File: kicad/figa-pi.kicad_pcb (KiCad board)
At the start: 4 copper layers, 65 x 56 mm, 158 parts, among them J1 BH-10(IDC-10MS), J2 PLS-2, J3 PBD-40(DS1023-2x20), J4 PLD-10(DS1021-2x5), J5 L829-1J1T-43, J6 POE connector, J7 PLS-1, J8 PLS-1, J9 PLS-1, U1 24LC32A/SN, U10 TLV62084DSGR, U11 TLV62084DSGR, U2 ASEMB-25.000MHZ-LC-T, U3 NUP4114UPXV6T1G, U5 10CL025ZE144, U6 KSZ9021GN, U7 CDCLVC1102PW, U9 TLV62084DSGR

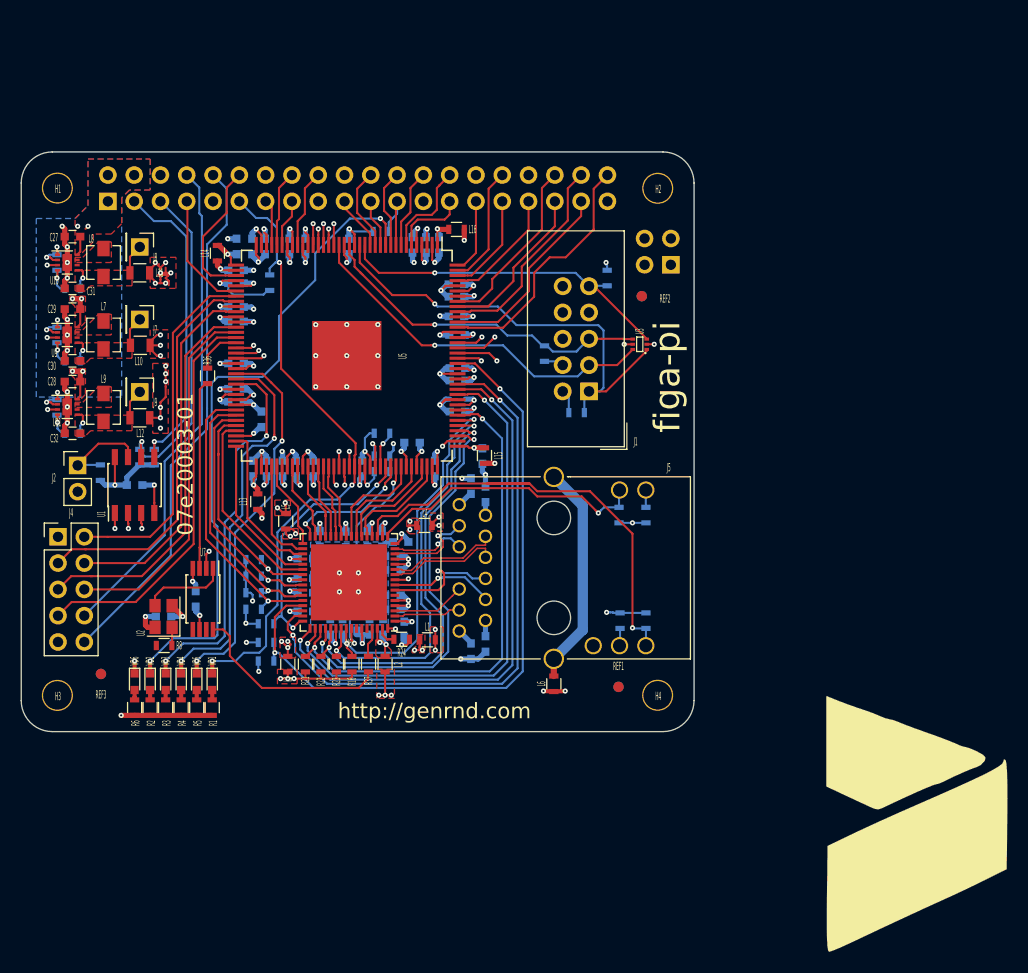
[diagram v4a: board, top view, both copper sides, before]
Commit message: Added logo as 2 footprints Corrected RefDes dimensions and placement on silk layers
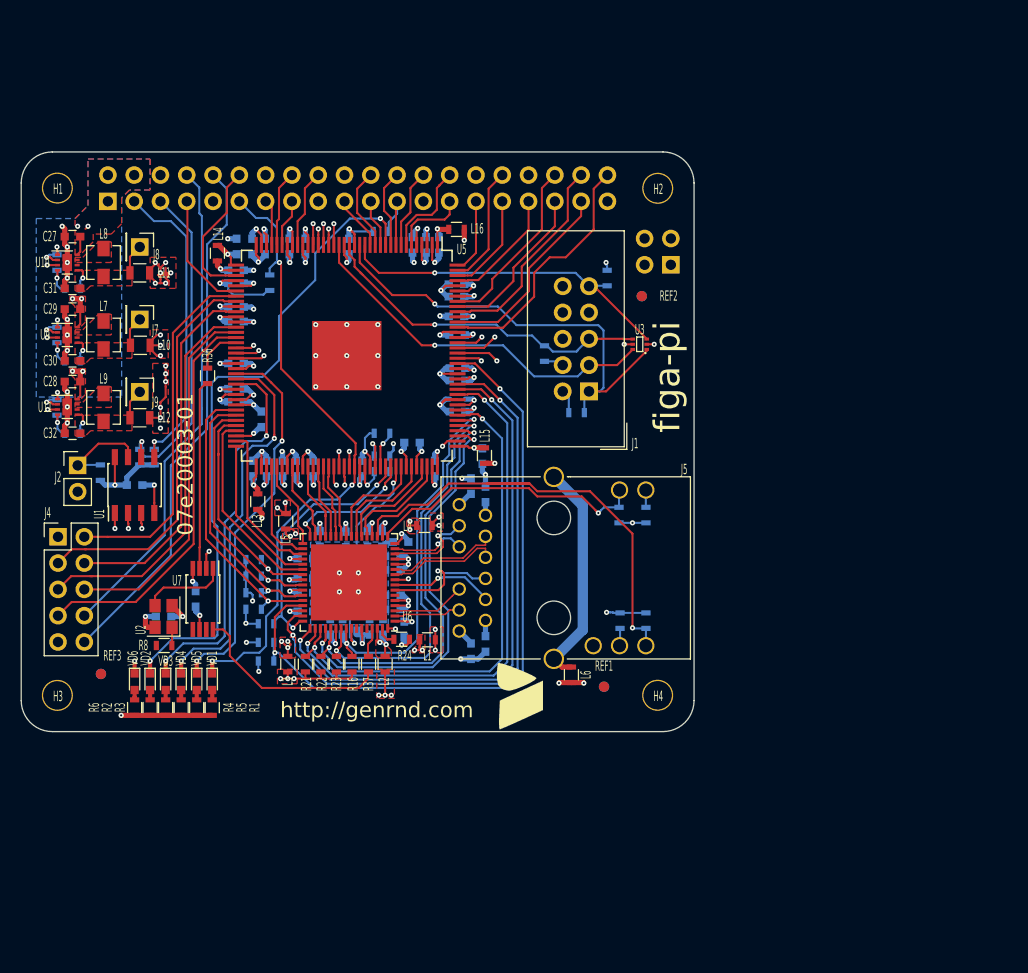
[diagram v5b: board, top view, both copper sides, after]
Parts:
- removed the G*** at (165.1, 125.7)
- added G***: LOGO, project_footprints:Logo_25_1, F.Cu at (126.3, 111.5)
- added G***: LOGO, project_footprints:Logo_25_2, F.Cu at (126.7, 114.1)
- moved L6 1.91 mm to (131.7, 111.3)
- moved REF1 1.40 mm to (134.8, 112.5)
- moved REF5 1.40 mm to (134.8, 112.5)
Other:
- rule pad_to_mask_clearance: 0.1 -> 0.05
- board text added: "This is a HAT compatible PCB starting design based on the official Raspberry Pi specs at: https://github.com/raspberrypi/hats/blob/master/designguide.md"
- board text removed: "If you want to use an SMT 40-pin header, please move the top edge up by 0.5mm and locate the header in the same location as the current TH part."
- board text removed: "This is a HAT compatible PCB starting design based on the official Raspberry Pi specs at: https://github.com/raspberrypi/hats/blob/master/designguide.md Currently the camera slot and display cutout are not here. See the schematic for the details on the EEPROM and power setup. This board does have the correct components for powering the Pi via the HAT. If you need the Pi to provide 5V or 3.3V, ple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"

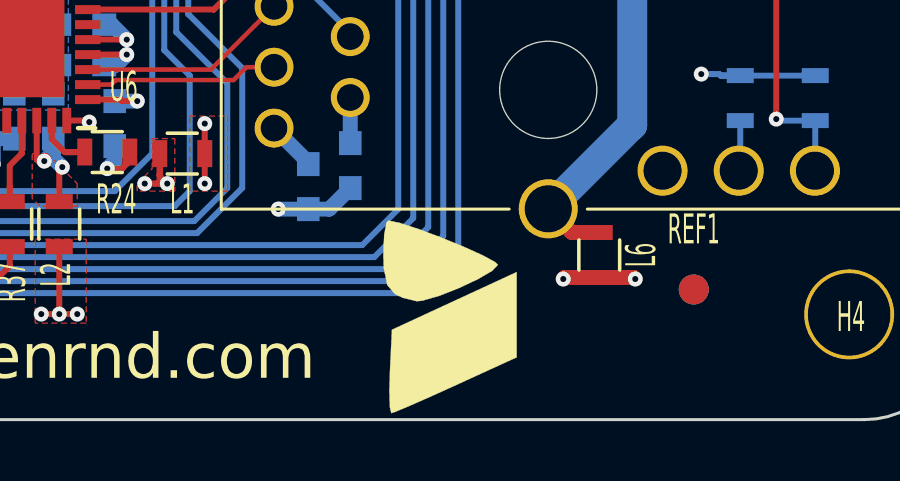
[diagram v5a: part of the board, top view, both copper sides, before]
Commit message: Updated Logo footprint Updated PCB with new footprint
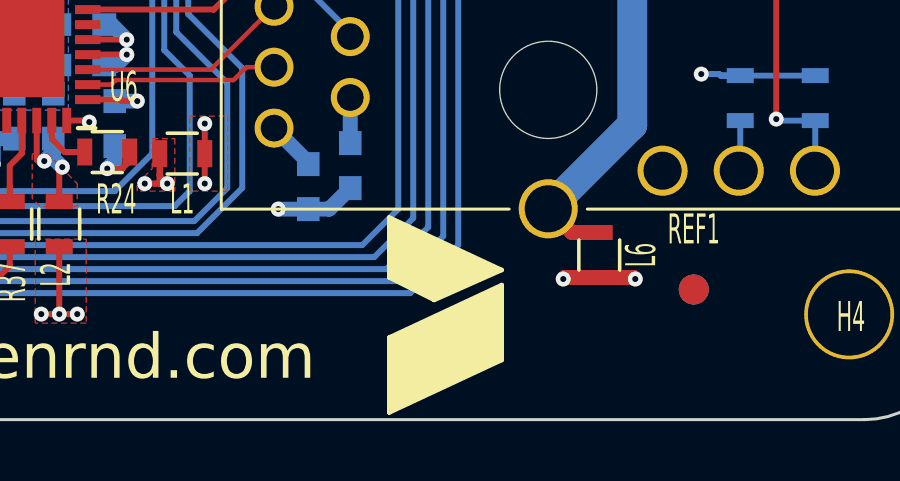
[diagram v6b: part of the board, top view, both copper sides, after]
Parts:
- removed the G*** at (126.3, 111.5)
- removed the G*** at (126.7, 114.1)
- added G***: LOGO, project_footprints:Logo, F.Cu at (126.7, 114.3)
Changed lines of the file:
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@@
     (links 0)
     (no_connects 0)
-    (area 69.386904 60.76761 155.363096 132.63)
+    (area 69.386904 60.76761 163.628715 132.63)
     (thickness 1.6)
     (drawings 56)
     (tracks 1844)
     (zones 0)
-    (modules 159)
+    (modules 158)
     (nets 149)
   )
@@
       (solder_mask_margin 0.77) (clearance 0.77))
   )
-  (module project_footprints:Logo_25_1 (layer F.Cu)
-    (at 126.3 111.53)
-    (fp_text reference G*** (at 0 0) (layer F.SilkS) hide
+  (module project_footprints:Logo (layer F.Cu)
+    (at 126.7 114.33)
+    (fp_text reference G*** (at 6.5 1.75) (layer F.SilkS) hide
       (effects (font (thickness 0.3)))
     )
-    (fp_text value LOGO (at 0.75 0) (layer F.SilkS) hide
+    (fp_text value LOGO (at 5.5 -0.5) (layer F.SilkS) hide
       (effects (font (thickness 0.3)))
     )
-    (fp_poly (pts (xy -1.255319 -1.270753) (xy -0.630766 -1.06857) (xy 0.117614 -0.789488) (xy 0.872331 -0.480872)
-      (xy 1.515897 -0.190086) (xy 1.930823 0.035504) (xy 2.022424 0.127222) (xy 1.831861 0.328167)
-      (xy 1.34976 0.608993) (xy 0.71153 0.90881) (xy 0.052583 1.166727) (xy -0.491671 1.321853)
-      (xy -0.678681 1.341837) (xy -1.149248 1.226891) (xy -1.404868 1.105889) (xy -1.665964 0.804232)
-      (xy -1.78346 0.227954) (xy -1.79823 -0.235948) (xy -1.769224 -0.873529) (xy -1.695134 -1.276107)
-      (xy -1.638558 -1.348672) (xy -1.255319 -1.270753)) (layer F.SilkS) (width 0.01))
-  )
-  (module project_footprints:Logo_25_2 (layer F.Cu)
-    (at 126.7 114.13)
-    (fp_text reference G*** (at 0 0) (layer F.SilkS) hide
-      (effects (font (thickness 0.3)))
-    )
-    (fp_text value LOGO (at 0.75 0) (layer F.SilkS) hide
-      (effects (font (thickness 0.3)))
-    )
-    (fp_poly (pts (xy 2.247788 0.610304) (xy 0.215173 1.541435) (xy -0.654945 1.935126) (xy -1.363337 2.24642)
-      (xy -1.81698 2.434959) (xy -1.930951 2.472566) (xy -1.980152 2.268378) (xy -1.99559 1.736208)
-      (xy -1.97754 1.081928) (xy -1.910619 -0.30871) (xy 0.168584 -1.269963) (xy 2.247788 -2.231215)
-      (xy 2.247788 0.610304)) (layer F.SilkS) (width 0.01))
+    (fp_line (start -0.5 -1.5) (end 1.75 -2.5) (layer F.SilkS) (width 0.15))
+    (fp_line (start -2 -2.5) (end -0.5 -1.75) (layer F.SilkS) (width 0.15))
+    (fp_line (start -2 -4.25) (end -2 -2.25) (layer F.SilkS) (width 0.15))
+    (fp_line (start 1.75 -2.5) (end -2 -4.25) (layer F.SilkS) (width 0.15))
+    (fp_line (start 1.75 0.5) (end 1.75 -2) (layer F.SilkS) (width 0.15))
+    (fp_line (start -2 2.25) (end 1.75 0.5) (layer F.SilkS) (width 0.15))
+    (fp_line (start -2 -0.25) (end -2 2.25) (layer F.SilkS) (width 0.15))
+    (fp_line (start 1.75 -2) (end -2 -0.25) (layer F.SilkS) (width 0.15))
+    (fp_poly (pts (xy 1.75 -2) (xy 1.75 0.5) (xy -2 2.25) (xy -2 -0.25)
+      (xy 1.75 -2)) (layer F.SilkS) (width 0.01))
+    (fp_poly (pts (xy -0.5 -1.5) (xy -2 -2.25) (xy -2 -4.25) (xy 1.75 -2.5)
+      (xy -0.5 -1.5)) (layer F.SilkS) (width 0.01))
+    (fp_line (start -0.5 -1.5) (end -2 -2.25) (layer F.SilkS) (width 0.15))
   )
   (gr_text http://genrnd.com (at 112.9 114.73) (layer F.SilkS)

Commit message: Updated PCB for manufacturing Created assembly drawings (without title) Created gerbers and drilling files
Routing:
- net +5V: track 11.5 -> 14.5 mm, vias 7 -> 9
- net +2V5: track 50.4 -> 52.4 mm
- net +1V2: track 52.9 -> 54.7 mm, vias 28 -> 29
- net (no net): track 0.35 -> 0.00 mm, vias 3 -> 0
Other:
- rule solder_mask_min_width: 0.15 -> 0.05

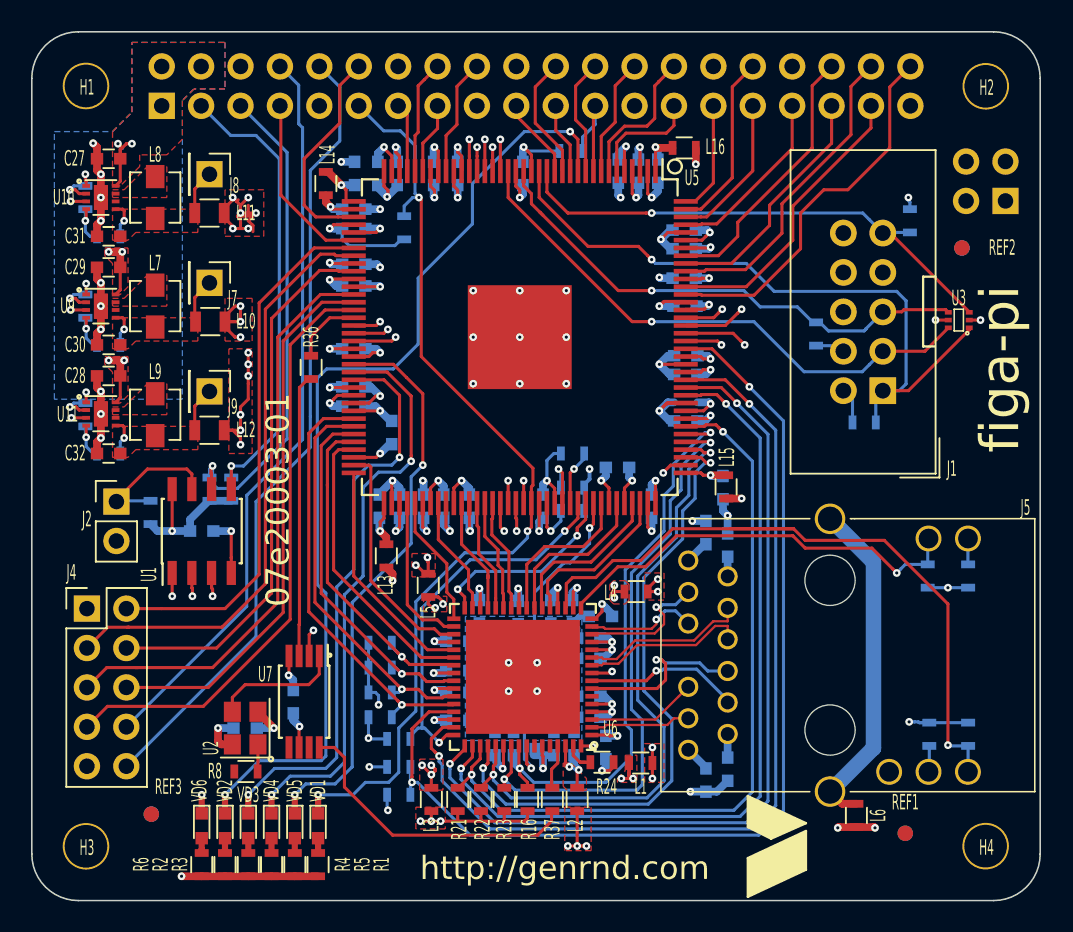
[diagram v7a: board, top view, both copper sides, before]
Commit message: Updated PCB for manufacturer "Rezonit" tech parameters Updated gerber and drill files Updated assembly drawing files Created mf_pcb folder Added files for manufacturer "Rezonit"
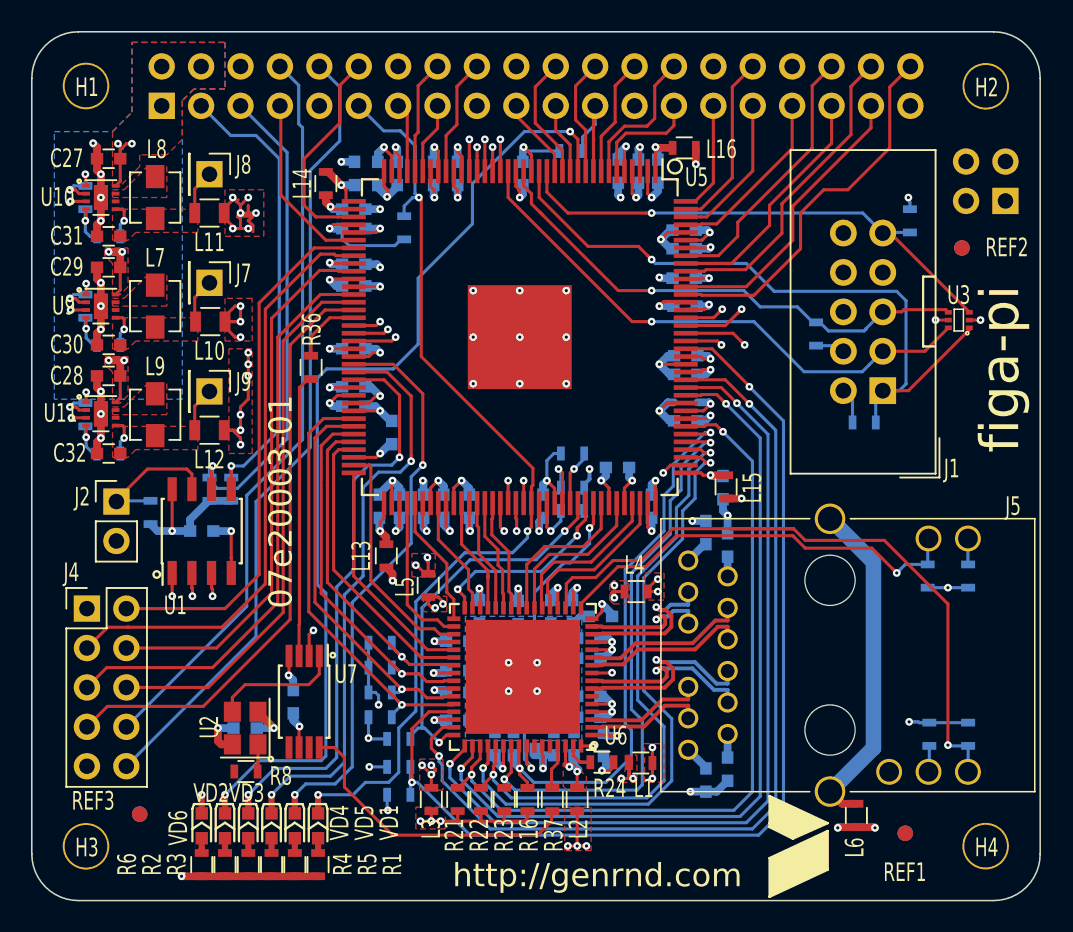
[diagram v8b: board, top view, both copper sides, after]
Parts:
- moved G*** 1.40 mm to (128.1, 114.3)
- moved REF3 0.75 mm to (85.5, 111.2) (x2)
- moved C18 0.25 mm to (115.4, 106.8)
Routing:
- net /ethernet.sch/TXRXB-: track 10.0 -> 12.4 mm
- net /ethernet.sch/TXRXD-: track 7.26 -> 9.03 mm
- net /ethernet.sch/TXRXD+: track 8.69 -> 10.4 mm
- net /ethernet.sch/TXRXB+: track 11.9 -> 13.5 mm
- net /ethernet.sch/TXRXA+: track 6.45 -> 7.60 mm
- net /ethernet.sch/TXRXA-: track 7.08 -> 7.60 mm
